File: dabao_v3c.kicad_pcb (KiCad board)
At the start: 2 copper layers, 21 x 41 mm, 51 parts, among them J1 USB_C_Receptacle_USB2.0_16P, SW1 SW_Push, SW2 SW_Push, U1 baochip1x, U3 Baochip, U4 MT3406, U5 EMS4000RSW, U6 MT3406, Y2 48.000MHz

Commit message: initial placement
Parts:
- removed FID1, FID2: Fiducial, common:IRIS fiducial 0.4mm
- removed FID3: Fiducial, common:IRIS fiducial2 0.4mm
- removed H1, H2, H3, H4: MountingHole, MountingHole:MountingHole_2.2mm_M2_DIN965
- removed U3: Baochip, common:Dabao_Vendor_Substrate
- added U2: ~, xiao:MOUDLE14P-XIAO-HALF-HOLE, F.Cu at (132.0, 70.0)
- R11: footprint Resistor_SMD:R_0402_1005Metric -> Resistor_SMD:R_0201_0603Metric
- SW1, SW2: value SW_Push -> SKTAAAE010; footprint common:SW_Push_1P1T_XKB_TS-1187A -> xiao:SW4-SMD-2.8-2.6X1.6X0.53MM
- Y2: footprint Crystal:Crystal_SMD_3225-4Pin_3.2x2.5mm -> Crystal:Crystal_SMD_2016-4Pin_2.0x1.6mm
- moved R2 21.4 mm to (138.2, 62.6)
- moved R4 20.7 mm to (138.4, 64.3)
- moved SW1 18.7 mm to (136.1, 79.1), turned to 0 degrees
- moved C13 18.0 mm to (137.8, 64.3)
- moved C10 13.9 mm to (129.8, 67.9), turned to 90 degrees
- moved C17 13.3 mm to (135.1, 76.3), turned to 180 degrees
- moved C11 12.7 mm to (131.6, 69.9), turned to 90 degrees
- moved C8 11.4 mm to (131.6, 71.6), turned to 90 degrees
- moved R3 11.2 mm to (126.0, 68.0), turned to -90 degrees
- moved Y2 11.1 mm to (128.0, 68.0), turned to 0 degrees
- moved C4 10.8 mm to (127.5, 69.7), turned to 0 degrees
- moved R9 10.6 mm to (132.6, 79.6), turned to 180 degrees
- moved L2 10.6 mm to (128.4, 75.6), turned to 180 degrees
- moved C16 10.6 mm to (128.3, 77.2), turned to 0 degrees
- moved U4 9.22 mm to (131.9, 76.9), turned to 90 degrees
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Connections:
- R2 pad 1: Net-(R2-Pad1) -> Net-(SW1-B0)
- SW1 pad 1: GND -> (no net)
- SW1 pad 2: Net-(R2-Pad1) -> (no net)
- SW2 pad 1: GND -> (no net)
- SW2 pad 2: /PC13 -> (no net)
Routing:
- net GND: track 81.7 -> 0.00 mm, vias 41 -> 0
- net /EN: track 62.5 -> 0.00 mm, vias 4 -> 0
- net /VSYS: track 51.7 -> 0.00 mm, vias 6 -> 0
- net /PC13: track 45.2 -> 0.00 mm, vias 2 -> 0
- net +3.3V: track 43.1 -> 0.00 mm, vias 10 -> 0
- net /RST_N: track 41.2 -> 0.00 mm, vias 6 -> 0
- net +0.9V: track 30.7 -> 0.00 mm, vias 4 -> 0
- net VBUS: track 25.1 -> 0.00 mm
- net /PB13: track 23.2 -> 0.00 mm
- net /PB14: track 21.3 -> 0.00 mm
- net /PB12: track 19.7 -> 0.00 mm
- net /PC0: track 19.7 -> 0.00 mm
- net /PC12: track 19.0 -> 0.00 mm
- net Net-(R2-Pad1): track 18.8 -> 0.00 mm
- net /PB11: track 18.2 -> 0.00 mm
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- removed copper zone on B.Cu, net +3.3V
- removed copper zone on F.Cu, net +3.3V
- removed copper zone on F.Cu, net /VSYS
- removed copper zone on B.Cu, net GND
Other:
- board size 21 x 41 mm -> 17.8 x 21.1 mm
- copper layers 2 -> 6

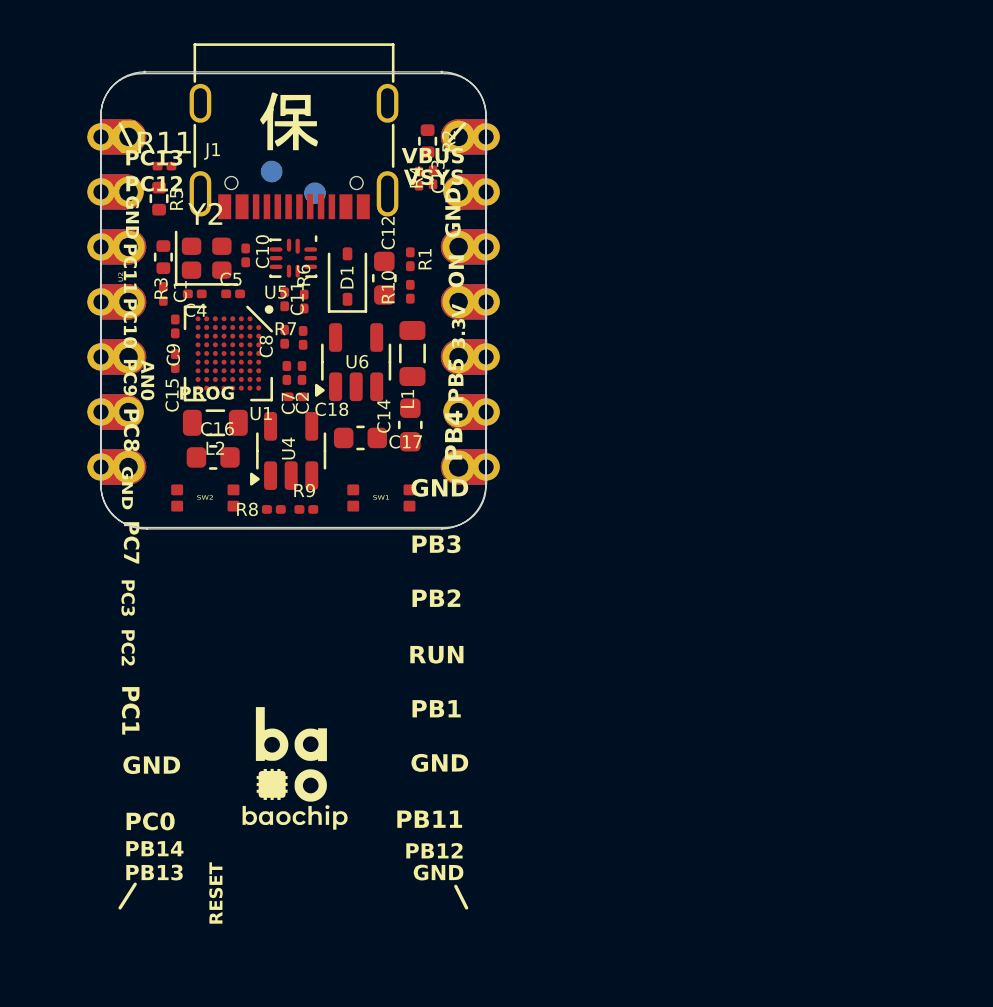
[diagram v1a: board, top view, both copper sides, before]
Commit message: some bunnie edits, battery charging added
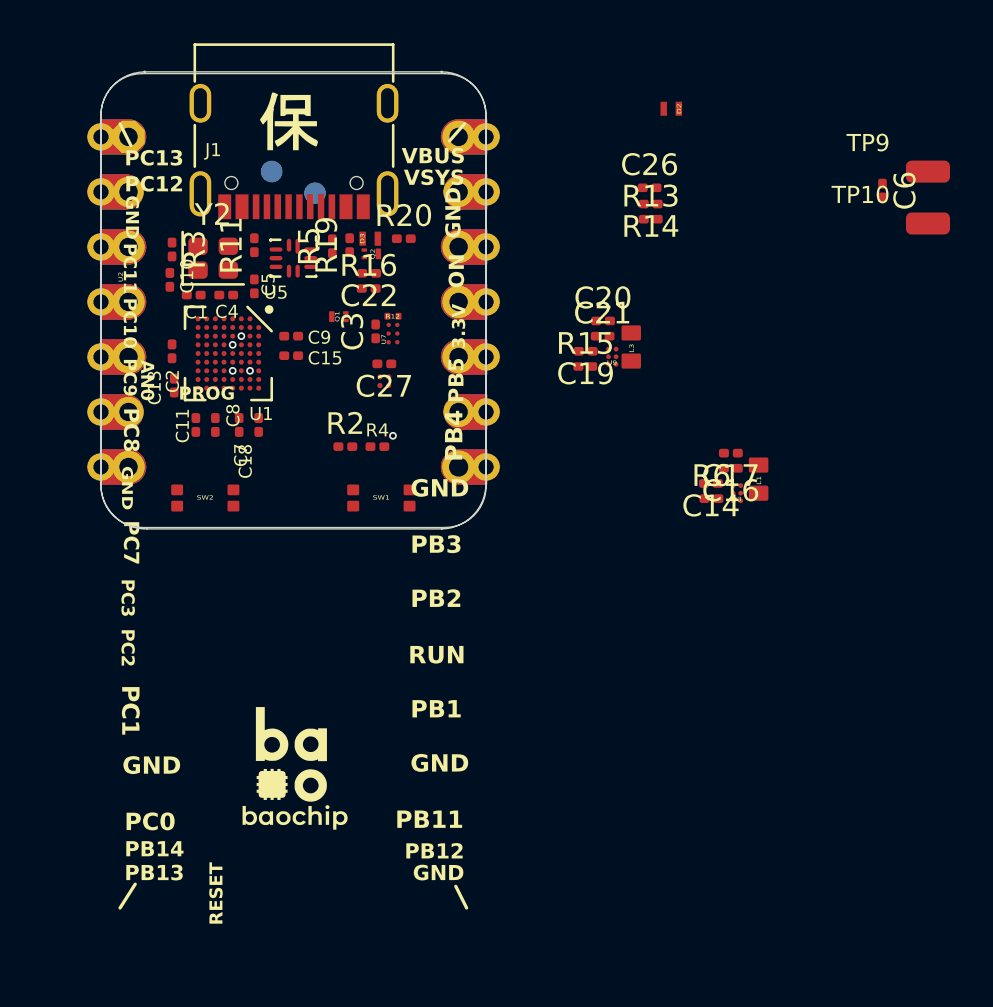
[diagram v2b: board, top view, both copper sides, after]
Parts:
- removed C12: 10uF, 25V, X5R, Capacitor_SMD:C_0603_1608Metric
- removed D1: 1N5819WS, Diode_SMD:D_SOD-323
- removed L2: 2.2uH MGFL2012F2R2MT-LF, Inductor_SMD:L_0805_2012Metric
- removed R1, R10: 10k, 1%, Resistor_SMD:R_0201_0603Metric
- removed R7: 453k, 1%, Resistor_SMD:R_0201_0603Metric
- removed R8: 100k, 1%, Resistor_SMD:R_0201_0603Metric
- removed R9: 43.2k, 1%, Resistor_SMD:R_0201_0603Metric
- removed U4, U6: MT3406, Package_TO_SOT_SMD:SOT-23-5
- added C19: 10uF, Capacitor_SMD:C_0201_0603Metric, F.Cu at (145.5, 72.3)
- added C20: 100nF, Capacitor_SMD:C_0201_0603Metric, F.Cu at (146.3, 70.9)
- added C21: 10uF, Capacitor_SMD:C_0201_0603Metric, F.Cu at (146.3, 71.6)
- added C22: 100nF, Capacitor_SMD:C_0201_0603Metric, F.Cu at (135.5, 68.7)
- added C26: 1nF, Capacitor_SMD:C_0201_0603Metric, F.Cu at (148.4, 64.8)
- added C27: 1uF, Capacitor_SMD:C_0201_0603Metric, F.Cu at (136.2, 72.9)
- added C3: 1uF, Capacitor_SMD:C_0201_0603Metric, F.Cu at (135.8, 71.4)
- added C6: 1uF, Capacitor_SMD:C_0201_0603Metric, F.Cu at (159.2, 64.9)
- added D2: LMBR4010BST5G, xiao:DFN1006-2L, F.Cu at (149.4, 61.1)
- added D3: LNZ8F5V6T5G, xiao:DFN1006-2L, F.Cu at (135.6, 67.1)
- added L3: 0.47uH, xiao:L0603, F.Cu at (147.6, 72.1)
- added Q1: LP0404N3T5G, xiao:PMOS_1.0X0.6X0.35MM, F.Cu at (134.1, 70.7)
- added Q2: LN237N3T5G, xiao:PMOS_1.0X0.6X0.35MM, F.Cu at (135.6, 67.8)
- added R12: 150K, xiao:R0201, F.Cu at (136.6, 70.7)
- added R13: 470K, Resistor_SMD:R_0201_0603Metric, F.Cu at (148.5, 66.2)
- added R14: 470K, Resistor_SMD:R_0201_0603Metric, F.Cu at (148.5, 65.5)
- added R15: 249K, Resistor_SMD:R_0201_0603Metric, F.Cu at (145.5, 73.0)
- added R16: 470K, Resistor_SMD:R_0201_0603Metric, F.Cu at (135.5, 69.4)
- added R19: 2.2K, Resistor_SMD:R_0201_0603Metric, F.Cu at (134.6, 67.4)
- added R20: 100R, Resistor_SMD:R_0201_0603Metric, F.Cu at (137.1, 67.1)
- added TP10: Test Point, xiao:TP-80X40MIL, F.Cu at (161.3, 66.4)
- added TP9: Test Point, xiao:TP-80X40MIL, F.Cu at (161.3, 64.0)
- added U3: SMD IC PMIC;DCDC Buck-ADJ-1A,Vin 1.95V to 5.5V,Vout 0.8V to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, xiao:BGA6-0.35-0.745X10.95X0.4MM, F.Cu at (152.5, 78.8)
- added U7: SGM40567-4.2XG/TR, xiao:WLCSP-0.4-0.92X1.16X0.4MM, F.Cu at (136.6, 71.5)
- added U8: SX1801CCR, xiao:WLCSP4-0.4-0.77X0.77X0.33MM, F.Cu at (136.2, 73.7)
- added U9: SMD IC PMIC;DCDC Buck-ADJ-1A,Vin 1.95V to 5.5V,Vout 1.8V to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, xiao:BGA6-0.35-0.745X10.95X0.4MM, F.Cu at (146.7, 72.5)
- C14, C17: value 10uF, 25V, X5R -> 10uF; footprint Capacitor_SMD:C_0603_1608Metric -> Capacitor_SMD:C_0201_0603Metric
- C16: value 10uF, 25V, X5R -> 100nF; footprint Capacitor_SMD:C_0603_1608Metric -> Capacitor_SMD:C_0201_0603Metric
- L1: value 2.2uH MGFL2012F2R2MT-LF -> 0.47uH; footprint Inductor_SMD:L_0805_2012Metric -> xiao:L0603
- R2, R3, R5: footprint Resistor_SMD:R_0402_1005Metric -> Resistor_SMD:R_0201_0603Metric
- R6: value 100k, 1% -> 12.1k
- moved C16 23.9 mm to (152.2, 77.7), turned to 180 degrees
- moved R6 20.9 mm to (151.3, 79.1), turned to 0 degrees
- moved C17 17.1 mm to (152.2, 77.0)
- moved L1 17.0 mm to (153.5, 78.2), turned to 90 degrees
- moved C13 14.8 mm to (126.5, 73.9), turned to -90 degrees
- moved R2 14.6 mm to (134.4, 76.7), turned to 0 degrees
- moved C14 14.1 mm to (151.3, 78.4), turned to 180 degrees
- moved R4 12.7 mm to (135.9, 76.7), turned to 180 degrees
- moved R5 8.30 mm to (133.8, 67.5)
- moved C11 7.10 mm to (127.5, 75.7), turned to -90 degrees
- moved C2 6.08 mm to (126.4, 72.3)
- moved R11 5.53 mm to (130.2, 67.4), turned to 90 degrees
- moved C9 5.37 mm to (131.9, 71.6), turned to 0 degrees
- moved C15 5.36 mm to (131.9, 72.5), turned to 0 degrees
- moved C8 5.18 mm to (128.4, 75.7), turned to -90 degrees
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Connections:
- C14 pad 1: +3.3V -> VSYS
- C16 pad 1: +0.9V -> +3.3V
- C17 pad 1: /VSYS -> +3.3V
- R6 pad 1: /FB_3.3V -> GND
- R6 pad 2: GND -> Net-(U3-MODE)
- SW1 pad 1: (no net) -> GND
- SW1 pad 2: (no net) -> GND
- SW1 pad 3: (no net) -> Net-(SW1-B0)
- SW1 pad 4: (no net) -> Net-(SW1-B0)
- SW2 pad 1: (no net) -> GND
- SW2 pad 2: (no net) -> GND
- SW2 pad 3: (no net) -> /PC13
- SW2 pad 4: (no net) -> /PC13
- U2 pad 1: /GPIO26/D0/ADC0 -> /PB3
- U2 pad 10: /GPIO4/D9/SPI0_MISO -> /PC2
- U2 pad 11: /GPIO3/D10/SPI0_MOSI -> /PC1
- U2 pad 12: +3V3 -> +3.3V
- U2 pad 2: /GPIO27/D1/ADC1 -> /PB4
- U2 pad 3: /GPIO28/D2/ADC2 -> /PB1
- U2 pad 4: /GPIO5/D3/SPI0_CS -> /PB2
- U2 pad 5: /GPIO6/D4/SDA1 -> /PB12
- U2 pad 6: /GPIO7/D5/SCL1 -> /PB11
- U2 pad 7: /GPIO0/D6/TX0 -> /PB14
- U2 pad 8: /GPIO1/D7/RX0 -> /PB13
- U2 pad 9: /GPIO2/D8/SPI0_SCK -> /PC0
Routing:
- net GND: vias 0 -> 3
- net +3.3V: vias 0 -> 2

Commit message: tentative bao layout
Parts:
- removed U2: ~, xiao:MOUDLE14P-XIAO-HALF-HOLE
- added R7: 5.1K, Resistor_SMD:R_0201_0603Metric, F.Cu at (137.2, 69.2)
- added U4: XIAO-HALF-HOLE-23P, xiao:MOUDLE23P-XIAO-HALF-HOLE, F.Cu at (132.0, 69.9)
- TP10, TP9: moved to B.Cu
- moved TP10 29.6 mm to (132.0, 70.9), turned to 180 degrees
- moved TP9 29.6 mm to (132.0, 68.5), turned to 180 degrees
- moved C6 25.3 mm to (134.2, 68.4), turned to 180 degrees
- moved L1 20.0 mm to (133.9, 74.0), turned to 180 degrees
- moved C17 19.1 mm to (133.2, 75.0)
- moved C16 19.1 mm to (133.2, 75.8)
- moved U3 18.3 mm to (134.5, 75.2), turned to 90 degrees
- moved R6 15.9 mm to (135.8, 75.4), turned to 180 degrees
- moved C14 15.9 mm to (135.8, 74.7), turned to 0 degrees
- moved D2 15.9 mm to (135.7, 69.0)
- moved C26 15.0 mm to (137.2, 74.6), turned to 180 degrees
- moved R14 14.0 mm to (137.2, 73.8), turned to 0 degrees
- moved R13 13.2 mm to (137.2, 73.0), turned to 180 degrees
- moved L3 12.7 mm to (134.9, 70.8), turned to 180 degrees
- moved C20 12.2 mm to (134.1, 71.8), turned to 180 degrees
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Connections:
- C16 pad 1: +3.3V -> +0.9V
- C17 pad 1: +3.3V -> +0.9V
- L1 pad 2: +3.3V -> +0.9V
- U1 pad B5: unconnected-(U1C-PB6-PadB5) -> /PA5
- U1 pad C4: GND -> /PA5
- U1 pad D7: +3.3V -> /PA7
- U1 pad E3: GND -> /PC5
- U1 pad E4: GND -> unconnected-(U1E-PF1-PadE4)
- U1 pad F2: unconnected-(U1E-PF8_PA1-PadF2) -> /PA1
- U1 pad F3: GND -> unconnected-(U1E-PA3-PadF3)
- U1 pad F4: GND -> /PC6
- U1 pad F6: +0.9V -> /PA6
- U1 pad G3: /PC9 -> /PA4
- U1 pad G5: unconnected-(U1E-PF4-PadG5) -> GND
- U1 pad G7: unconnected-(U1E-PF5-PadG7) -> +0.9V
- U3 pad A2: +3.3V -> +0.9V
- U7 pad B2: NCHG -> Net-(U7-NCHG)
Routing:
- net VBUS: track 0.00 -> 22.9 mm
- net /PC1: track 0.00 -> 16.5 mm, vias 0 -> 1
- net /PC2: track 0.00 -> 14.8 mm, vias 0 -> 1
- net /PB13: track 0.00 -> 14.4 mm, vias 0 -> 1
- net /PA4: track 0.00 -> 13.8 mm, vias 0 -> 1
- net /PC0: track 0.00 -> 12.7 mm, vias 0 -> 1
- net /PB2: track 0.00 -> 12.5 mm, vias 0 -> 1
- net /PC6: track 0.00 -> 12.1 mm, vias 0 -> 1
- net /PA1: track 0.00 -> 11.1 mm, vias 0 -> 2
- net /PA5: track 0.00 -> 11.0 mm, vias 0 -> 1
- net /PB1: track 0.00 -> 10.6 mm, vias 0 -> 1
- net /PC5: track 0.00 -> 10.1 mm, vias 0 -> 1
- net +0.9V: track 0.00 -> 9.93 mm, vias 0 -> 4
- net /PA6: track 0.00 -> 9.01 mm, vias 0 -> 1
- net /PA7: track 0.00 -> 7.87 mm, vias 0 -> 1
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- added copper zone on In3.Cu, net +3.3V
- added copper zone on B.Cu, net GND
- added copper zone on F.Cu, net GND
- added copper zone on In1.Cu, net GND

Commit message: clean DRC v1
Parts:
- moved TP10 5.89 mm to (136.5, 67.1), turned to 0 degrees
- moved TP9 4.81 mm to (136.7, 69.5)
- moved C6 1.58 mm to (135.7, 68.9)
- moved R20 1.53 mm to (134.2, 69.5), turned to 0 degrees
- moved D2 1.50 mm to (134.2, 68.6), turned to 180 degrees
- moved Q1 1.13 mm to (135.7, 69.7), turned to -90 degrees
- moved TP2 0.87 mm to (133.6, 64.3), turned to 90 degrees
- moved TP1 0.55 mm to (130.4, 64.0), turned to 90 degrees
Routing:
- net /RST_N: track 2.00 -> 15.4 mm, vias 0 -> 2
- net /PC13: track 5.51 -> 16.4 mm, vias 2 -> 3
- net Net-(SW1-B0): track 0.73 -> 8.31 mm
- net +3.3V: track 6.92 -> 12.0 mm, vias 4 -> 8
- net GND: track 2.33 -> 7.20 mm, vias 4 -> 19
- net /XO_48M: track 4.61 -> 8.88 mm
- net VSYS: track 0.73 -> 3.69 mm, vias 1 -> 6
- net VBUS: track 22.9 -> 25.7 mm, vias 0 -> 2
- net VBAT: track 1.53 -> 3.94 mm, vias 0 -> 1
- net /USBCONN_P: track 4.55 -> 6.68 mm
- net /PA4: track 13.8 -> 11.9 mm
- net /PC2: track 14.8 -> 16.5 mm
- net /PA1: track 11.1 -> 9.34 mm
- net /PA6: track 9.01 -> 10.7 mm
- net /PA7: track 7.87 -> 9.40 mm
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- added copper zone on In4.Cu, net +0.9V
- added copper zone on In2.Cu, net GND
- added copper zone on In3.Cu, net GND
- added copper zone on In4.Cu, net GND
- added copper zone on In4.Cu, net VSYS

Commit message: now with more pins
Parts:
- removed the G*** at (132.0, 68.5)
- added TP3: TEST-POINT'4545', xiao:TP-D45MIL, B.Cu at (133.3, 63.7)
- added TP4: TEST-POINT'4545', xiao:TP-D45MIL, B.Cu at (130.7, 63.7)
- added TP5: TEST-POINT'4545', xiao:TP-D45MIL, B.Cu at (133.3, 66.2)
- added TP6: TEST-POINT'4545', xiao:TP-D45MIL, B.Cu at (130.7, 66.2)
- added TP7: TEST-POINT'4545', xiao:TP-D45MIL, B.Cu at (133.3, 68.8)
- added TP8: TEST-POINT'4545', xiao:TP-D45MIL, B.Cu at (130.7, 68.8)
- G***: moved to B.Cu
- TP1, TP2: value TestPoint -> TEST-POINT'4545'; footprint TestPoint:TestPoint_Pad_D1.0mm -> xiao:TP-D45MIL
- moved G*** 15.6 mm to (131.7, 76.0), turned to 180 degrees
- moved TP2 4.25 mm to (130.7, 61.2), turned to -90 degrees
- moved TP1 4.01 mm to (133.3, 61.2), turned to -90 degrees
- moved R5 0.06 mm to (133.9, 67.5)
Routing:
- net /PC11: track 0.00 -> 15.6 mm, vias 0 -> 1
- net /PC10: track 0.00 -> 13.0 mm, vias 0 -> 1
- net /PB4: track 0.00 -> 10.1 mm, vias 0 -> 2
- net /PB3: track 0.00 -> 9.57 mm, vias 0 -> 2
- net GND: track 7.20 -> 8.91 mm, vias 19 -> 23
- net VBUS: track 25.7 -> 27.1 mm
- net +3.3V: track 12.0 -> 13.0 mm, vias 8 -> 11
- net /PA5: track 11.7 -> 12.5 mm
- net /PC5: track 9.16 -> 9.90 mm
- net /USBCONN_N: track 5.73 -> 6.32 mm
- net /PA1: track 9.34 -> 9.87 mm
- net +0.9V: track 9.38 -> 9.59 mm, vias 3 -> 4
- net /PC6: track 12.1 -> 12.0 mm, vias 1 -> 2
- added copper zone on In4.Cu, net +3.3V
- removed copper zone on In3.Cu, net GND
- removed copper zone on In4.Cu, net GND

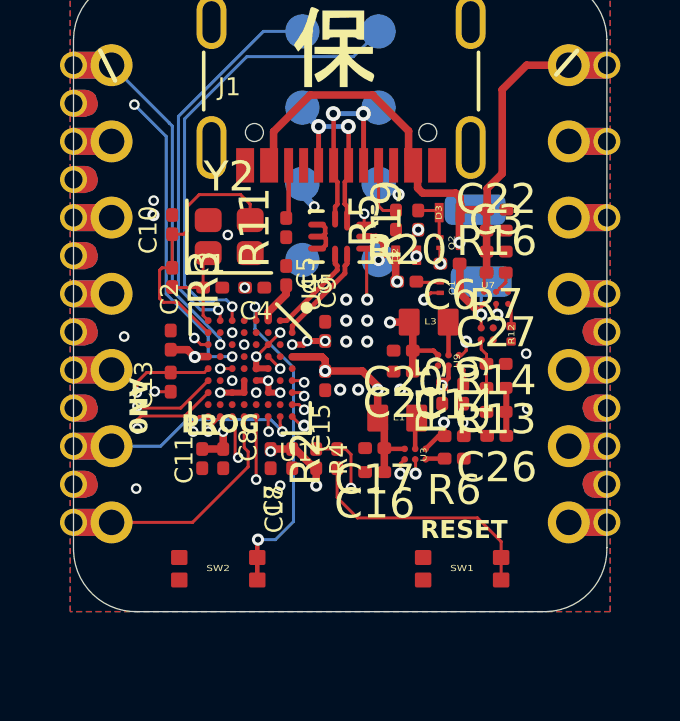
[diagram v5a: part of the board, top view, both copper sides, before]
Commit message: clean-drc, now more pads
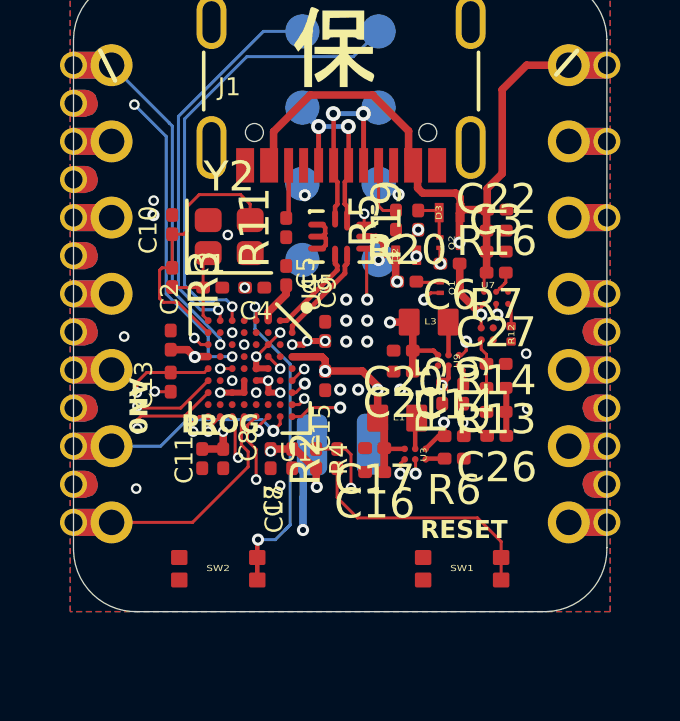
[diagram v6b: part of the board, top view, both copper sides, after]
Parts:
- moved TP10 8.54 mm to (133.1, 74.9), turned to 90 degrees
- moved TP9 7.84 mm to (131.1, 74.9), turned to -90 degrees
- moved G*** 4.18 mm to (130.4, 80.0)
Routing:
- net VBAT: track 3.94 -> 18.5 mm, vias 1 -> 2
- net /PB3: track 9.57 -> 8.49 mm
- net /PB2: track 12.3 -> 11.3 mm
- net /PB13: track 15.3 -> 14.4 mm
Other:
- board text added: "3V3"
- board text added: "BAT"
- board text added: "D+"
- board text added: "D-"
- board text added: "D0"
- board text added: "D1"
- board text added: "D10"
- board text added: "D2"
- board text added: "D3"
- board text added: "D4"
- board text added: "D5"
- board text added: "D6"
- board text added: "D7"
- board text added: "D8"
- board text added: "D9"
- board text added: "VUSB"
- board text removed: "3.3V"
- board text removed: "ON"
- board text removed: "PB1"
- board text removed: "PB11"
- board text removed: "PB12"
- board text removed: "PB13"
- board text removed: "PB14"
- board text removed: "PB2"
- board text removed: "PB3"
- board text removed: "PB4"
- board text removed: "PB5"
- board text removed: "PC0"
- board text removed: "PC1"
- board text removed: "PC10"
- board text removed: "PC11"
- board text removed: "PC12"
- board text removed: "PC13"
- board text removed: "PC2"
- board text removed: "PC3"
- board text removed: "PC7"
- board text removed: "PC8"
- board text removed: "PC9"
- board text removed: "RUN"
- board text removed: "U+"
- board text removed: "U-"
- board text removed: "VBUS"
- board text removed: "VSYS"

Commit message: now with silk and logos and an led
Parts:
- removed the G*** at (130.4, 80.0)
- added D1: WS2812B-1010, xiao:1010 RGB WS2812B, F.Cu at (125.8, 60.7)
- added G***: LOGO, xiao:simplebaologo, B.Cu at (132.1, 71.6)
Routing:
- net VSYS: track 3.69 -> 20.6 mm, vias 6 -> 7
- net /PC12: track 0.00 -> 12.3 mm, vias 0 -> 2
- net (no net): track 0.00 -> 0.91 mm
- net /PB3: track 8.49 -> 7.81 mm
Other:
- board text added: "+"
- board text added: "PB3"
- board text added: "PB4"
- board text added: "PC10"
- board text added: "PC11"
- board text added: "samchin"
- board text added: "winter'27"
- board text added: "xiao bao v1"
- board text removed: "AN0"
- board text removed: "Remove PCB material from these four boxes"
- board text removed: "V-score attached only in this middle region"
- board text removed: "V-score line"
- board text removed: "bunnie"
- board text removed: "v3c 11/25"
